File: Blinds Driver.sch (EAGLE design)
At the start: 22 parts

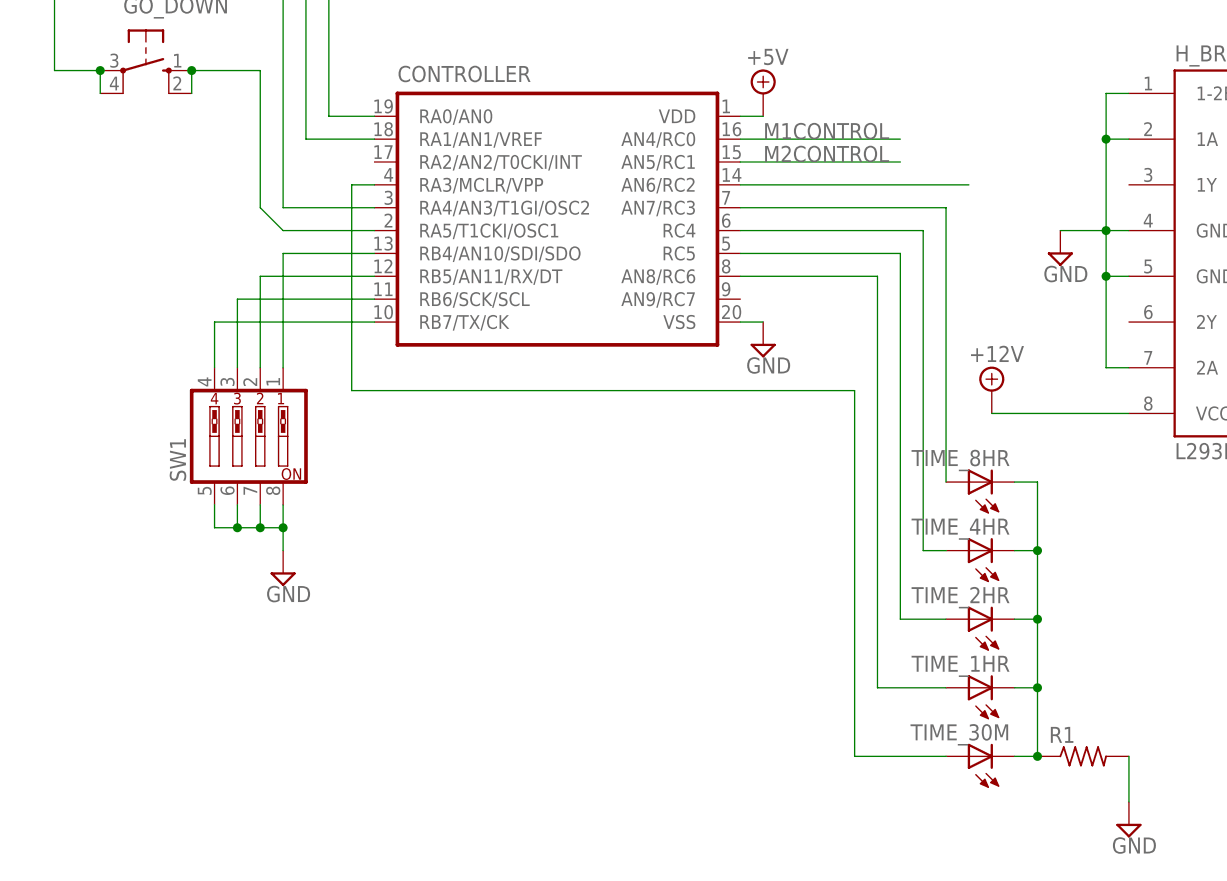
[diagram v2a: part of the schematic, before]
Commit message: Pin A3 is input-only, so use C7 instead
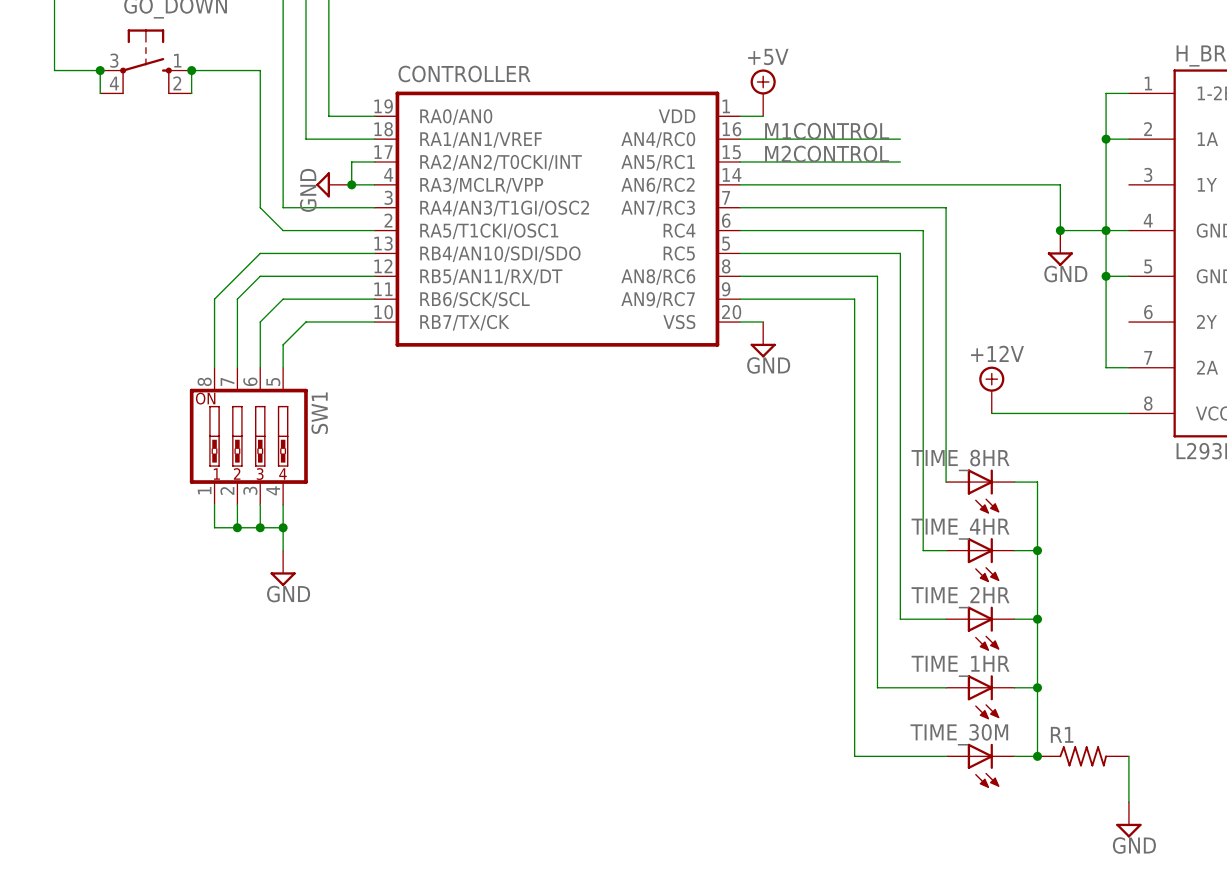
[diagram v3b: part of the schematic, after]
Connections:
- removed net N$2: CONTROLLER.AN6/RC2
- removed net N$9: CONTROLLER.RB7/TX/CK, SW1.4
- new net N$1: CONTROLLER.RB7/TX/CK, SW1.5
- net GND: now also CONTROLLER.AN6/RC2, CONTROLLER.RA2/AN2/T0CKI/INT, CONTROLLER.RA3/MCLR/VPP, SW1.1, SW1.2, SW1.3, SW1.4; no longer SW1.5, SW1.6, SW1.7, SW1.8
- net N$24: now also CONTROLLER.AN9/RC7; no longer CONTROLLER.RA3/MCLR/VPP
- net N$4: now also CONTROLLER.RB6/SCK/SCL, SW1.6; no longer CONTROLLER.RB4/AN10/SDI/SDO, SW1.1
- net N$5: now also SW1.7; no longer SW1.2
- net N$7: now also CONTROLLER.RB4/AN10/SDI/SDO, SW1.8; no longer CONTROLLER.RB6/SCK/SCL, SW1.3
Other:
- moved on the sheet: SW1
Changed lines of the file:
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@@
 <part name="SUPPLY16" library="supply2" deviceset="+5V" device=""/>
 <part name="SUPPLY19" library="supply2" deviceset="GND" device=""/>
+<part name="SUPPLY20" library="supply2" deviceset="GND" device=""/>
 </parts>
 <sheets>
@@
 <instance part="SUPPLY18" gate="+12V" x="106.68" y="86.36"/>
 <instance part="SUPPLY21" gate="+12V" x="99.06" y="86.36"/>
-<instance part="SW1" gate="A" x="-55.88" y="38.1" rot="R90"/>
+<instance part="SW1" gate="A" x="-53.34" y="38.1" rot="R270"/>
 <instance part="M" gate="-1" x="119.38" y="66.04"/>
 <instance part="M" gate="-2" x="119.38" y="63.5"/>
@@
 <instance part="SUPPLY16" gate="+5V" x="48.26" y="109.22"/>
 <instance part="SUPPLY19" gate="GND" x="43.18" y="93.98"/>
+<instance part="SUPPLY20" gate="GND" x="-45.72" y="66.04" rot="R270"/>
 </instances>
 <busses>
@@
 <pinref part="SUPPLY12" gate="GND" pin="GND"/>
 <wire x1="-50.8" y1="25.4" x2="-50.8" y2="27.94" width="0.1524" layer="91"/>
-<wire x1="-50.8" y1="27.94" x2="-50.8" y2="30.48" width="0.1524" layer="91"/>
+<wire x1="-58.42" y1="27.94" x2="-55.88" y2="27.94" width="0.1524" layer="91"/>
+<pinref part="SW1" gate="A" pin="1"/>
+<wire x1="-55.88" y1="27.94" x2="-53.34" y2="27.94" width="0.1524" layer="91"/>
+<wire x1="-53.34" y1="27.94" x2="-50.8" y2="27.94" width="0.1524" layer="91"/>
+<wire x1="-58.42" y1="30.48" x2="-58.42" y2="27.94" width="0.1524" layer="91"/>
+<pinref part="SW1" gate="A" pin="2"/>
+<wire x1="-55.88" y1="30.48" x2="-55.88" y2="27.94" width="0.1524" layer="91"/>
+<pinref part="SW1" gate="A" pin="3"/>
 <wire x1="-53.34" y1="30.48" x2="-53.34" y2="27.94" width="0.1524" layer="91"/>
-<wire x1="-53.34" y1="27.94" x2="-50.8" y2="27.94" width="0.1524" layer="91"/>
-<wire x1="-55.88" y1="30.48" x2="-55.88" y2="27.94" width="0.1524" layer="91"/>
-<wire x1="-55.88" y1="27.94" x2="-53.34" y2="27.94" width="0.1524" layer="91"/>
-<wire x1="-58.42" y1="30.48" x2="-58.42" y2="27.94" width="0.1524" layer="91"/>
-<wire x1="-58.42" y1="27.94" x2="-55.88" y2="27.94" width="0.1524" layer="91"/>
+<pinref part="SW1" gate="A" pin="4"/>
+<wire x1="-50.8" y1="30.48" x2="-50.8" y2="27.94" width="0.1524" layer="91"/>
+<junction x="-55.88" y="27.94"/>
+<junction x="-53.34" y="27.94"/>
 <junction x="-50.8" y="27.94"/>
-<junction x="-53.34" y="27.94"/>
-<junction x="-55.88" y="27.94"/>
-<pinref part="SW1" gate="A" pin="5"/>
-<pinref part="SW1" gate="A" pin="6"/>
-<pinref part="SW1" gate="A" pin="7"/>
-<pinref part="SW1" gate="A" pin="8"/>
 </segment>
 <segment>
@@
 <wire x1="40.64" y1="45.72" x2="43.18" y2="45.72" width="0.1524" layer="91"/>
 <junction x="40.64" y="55.88"/>
+<pinref part="CONTROLLER" gate="G$1" pin="AN6/RC2"/>
+<wire x1="0" y1="66.04" x2="35.56" y2="66.04" width="0.1524" layer="91"/>
+<wire x1="35.56" y1="66.04" x2="35.56" y2="60.96" width="0.1524" layer="91"/>
+<junction x="35.56" y="60.96"/>
 </segment>
 <segment>
@@
 <junction x="43.18" y="96.52"/>
 </segment>
-</net>
-<net name="N$2" class="0">
-<segment>
-<pinref part="CONTROLLER" gate="G$1" pin="AN6/RC2"/>
-<wire x1="0" y1="66.04" x2="25.4" y2="66.04" width="0.1524" layer="91"/>
+<segment>
+<pinref part="CONTROLLER" gate="G$1" pin="RA3/MCLR/VPP"/>
+<pinref part="SUPPLY20" gate="GND" pin="GND"/>
+<wire x1="-40.64" y1="66.04" x2="-43.18" y2="66.04" width="0.1524" layer="91"/>
+<wire x1="-43.18" y1="66.04" x2="-43.18" y2="68.58" width="0.1524" layer="91"/>
+<pinref part="CONTROLLER" gate="G$1" pin="RA2/AN2/T0CKI/INT"/>
+<wire x1="-43.18" y1="68.58" x2="-40.64" y2="68.58" width="0.1524" layer="91"/>
+<junction x="-43.18" y="66.04"/>
 </segment>
 </net>
@@
 <net name="N$24" class="0">
 <segment>
-<pinref part="CONTROLLER" gate="G$1" pin="RA3/MCLR/VPP"/>
-<wire x1="-40.64" y1="66.04" x2="-43.18" y2="66.04" width="0.1524" layer="91"/>
-<wire x1="-43.18" y1="66.04" x2="-43.18" y2="43.18" width="0.1524" layer="91"/>
-<wire x1="-43.18" y1="43.18" x2="12.7" y2="43.18" width="0.1524" layer="91"/>
-<wire x1="12.7" y1="43.18" x2="12.7" y2="2.54" width="0.1524" layer="91"/>
+<wire x1="12.7" y1="53.34" x2="12.7" y2="2.54" width="0.1524" layer="91"/>
 <pinref part="TIME_30M" gate="G$1" pin="A"/>
 <wire x1="12.7" y1="2.54" x2="22.86" y2="2.54" width="0.1524" layer="91"/>
-</segment>
-</net>
-<net name="N$4" class="0">
-<segment>
-<wire x1="-50.8" y1="45.72" x2="-50.8" y2="58.42" width="0.1524" layer="91"/>
-<pinref part="CONTROLLER" gate="G$1" pin="RB4/AN10/SDI/SDO"/>
-<wire x1="-50.8" y1="58.42" x2="-40.64" y2="58.42" width="0.1524" layer="91"/>
-<pinref part="SW1" gate="A" pin="1"/>
-</segment>
-</net>
-<net name="N$5" class="0">
-<segment>
-<pinref part="CONTROLLER" gate="G$1" pin="RB5/AN11/RX/DT"/>
-<wire x1="-40.64" y1="55.88" x2="-53.34" y2="55.88" width="0.1524" layer="91"/>
-<wire x1="-53.34" y1="55.88" x2="-53.34" y2="45.72" width="0.1524" layer="91"/>
-<pinref part="SW1" gate="A" pin="2"/>
-</segment>
-</net>
-<net name="N$7" class="0">
-<segment>
-<pinref part="CONTROLLER" gate="G$1" pin="RB6/SCK/SCL"/>
-<wire x1="-40.64" y1="53.34" x2="-55.88" y2="53.34" width="0.1524" layer="91"/>
-<wire x1="-55.88" y1="53.34" x2="-55.88" y2="45.72" width="0.1524" layer="91"/>
-<pinref part="SW1" gate="A" pin="3"/>
-</segment>
-</net>
-<net name="N$9" class="0">
-<segment>
-<pinref part="CONTROLLER" gate="G$1" pin="RB7/TX/CK"/>
-<wire x1="-40.64" y1="50.8" x2="-58.42" y2="50.8" width="0.1524" layer="91"/>
-<wire x1="-58.42" y1="50.8" x2="-58.42" y2="45.72" width="0.1524" layer="91"/>
-<pinref part="SW1" gate="A" pin="4"/>
+<pinref part="CONTROLLER" gate="G$1" pin="AN9/RC7"/>
+<wire x1="12.7" y1="53.34" x2="0" y2="53.34" width="0.1524" layer="91"/>
 </segment>
 </net>
@@
 </segment>
 </net>
+<net name="N$1" class="0">
+<segment>
+<wire x1="-50.8" y1="48.26" x2="-48.26" y2="50.8" width="0.1524" layer="91"/>
+<pinref part="CONTROLLER" gate="G$1" pin="RB7/TX/CK"/>
+<wire x1="-48.26" y1="50.8" x2="-40.64" y2="50.8" width="0.1524" layer="91"/>
+<pinref part="SW1" gate="A" pin="5"/>
+<wire x1="-50.8" y1="48.26" x2="-50.8" y2="45.72" width="0.1524" layer="91"/>
+</segment>
+</net>
+<net name="N$4" class="0">
+<segment>
+<pinref part="CONTROLLER" gate="G$1" pin="RB6/SCK/SCL"/>
+<wire x1="-40.64" y1="53.34" x2="-50.8" y2="53.34" width="0.1524" layer="91"/>
+<wire x1="-50.8" y1="53.34" x2="-53.34" y2="50.8" width="0.1524" layer="91"/>
+<pinref part="SW1" gate="A" pin="6"/>
+<wire x1="-53.34" y1="50.8" x2="-53.34" y2="45.72" width="0.1524" layer="91"/>
+</segment>
+</net>
+<net name="N$5" class="0">
+<segment>
+<pinref part="CONTROLLER" gate="G$1" pin="RB5/AN11/RX/DT"/>
+<wire x1="-40.64" y1="55.88" x2="-53.34" y2="55.88" width="0.1524" layer="91"/>
+<wire x1="-53.34" y1="55.88" x2="-55.88" y2="53.34" width="0.1524" layer="91"/>
+<pinref part="SW1" gate="A" pin="7"/>
+<wire x1="-55.88" y1="53.34" x2="-55.88" y2="45.72" width="0.1524" layer="91"/>
+</segment>
+</net>
+<net name="N$7" class="0">
+<segment>
+<pinref part="CONTROLLER" gate="G$1" pin="RB4/AN10/SDI/SDO"/>
+<wire x1="-40.64" y1="58.42" x2="-53.34" y2="58.42" width="0.1524" layer="91"/>
+<wire x1="-53.34" y1="58.42" x2="-58.42" y2="53.34" width="0.1524" layer="91"/>
+<pinref part="SW1" gate="A" pin="8"/>
+<wire x1="-58.42" y1="53.34" x2="-58.42" y2="45.72" width="0.1524" layer="91"/>
+</segment>
+</net>
